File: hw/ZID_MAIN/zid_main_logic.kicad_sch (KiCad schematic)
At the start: 82 parts, among them J1 Conn_01x02_Pin_2.54mm, J2 Conn_02x05_2.54mm, J3 Conn_02x05_2.54mm, J4 Conn_02x05_PINHDR_2.54mm, J5 HDR 1x04 Socket, J6 Conn_02x03_Odd_Even, J7 Conn_01x03, M1 WS-RP2040-Zero, SW1 SW_Push, SW2 SW_DIP_x02, U1 74HCT161, U10 74FCT2245, U11 SST39SF010, U12 AS7C1024B-10J, U13 74FCT541C, U14 74AHCT244, U15 74FCT257T, U16 74HCT166, U17 74HCT166, U18 74LVC245, U19 74LVC125AS, U2 74FCT541C, U20 24LC32, U21 ATF1504AS-44T, U22 74AHCT1G125, U23 74LVC273, U25 74LVC3G04, U3 74FCT541C, U4 MIC2775, U5 OSC-20MHz, U6 Z80 C20MHz-PLCC, U7 ATF1508AS, U8 74FCT2245, U9 74FCT2245

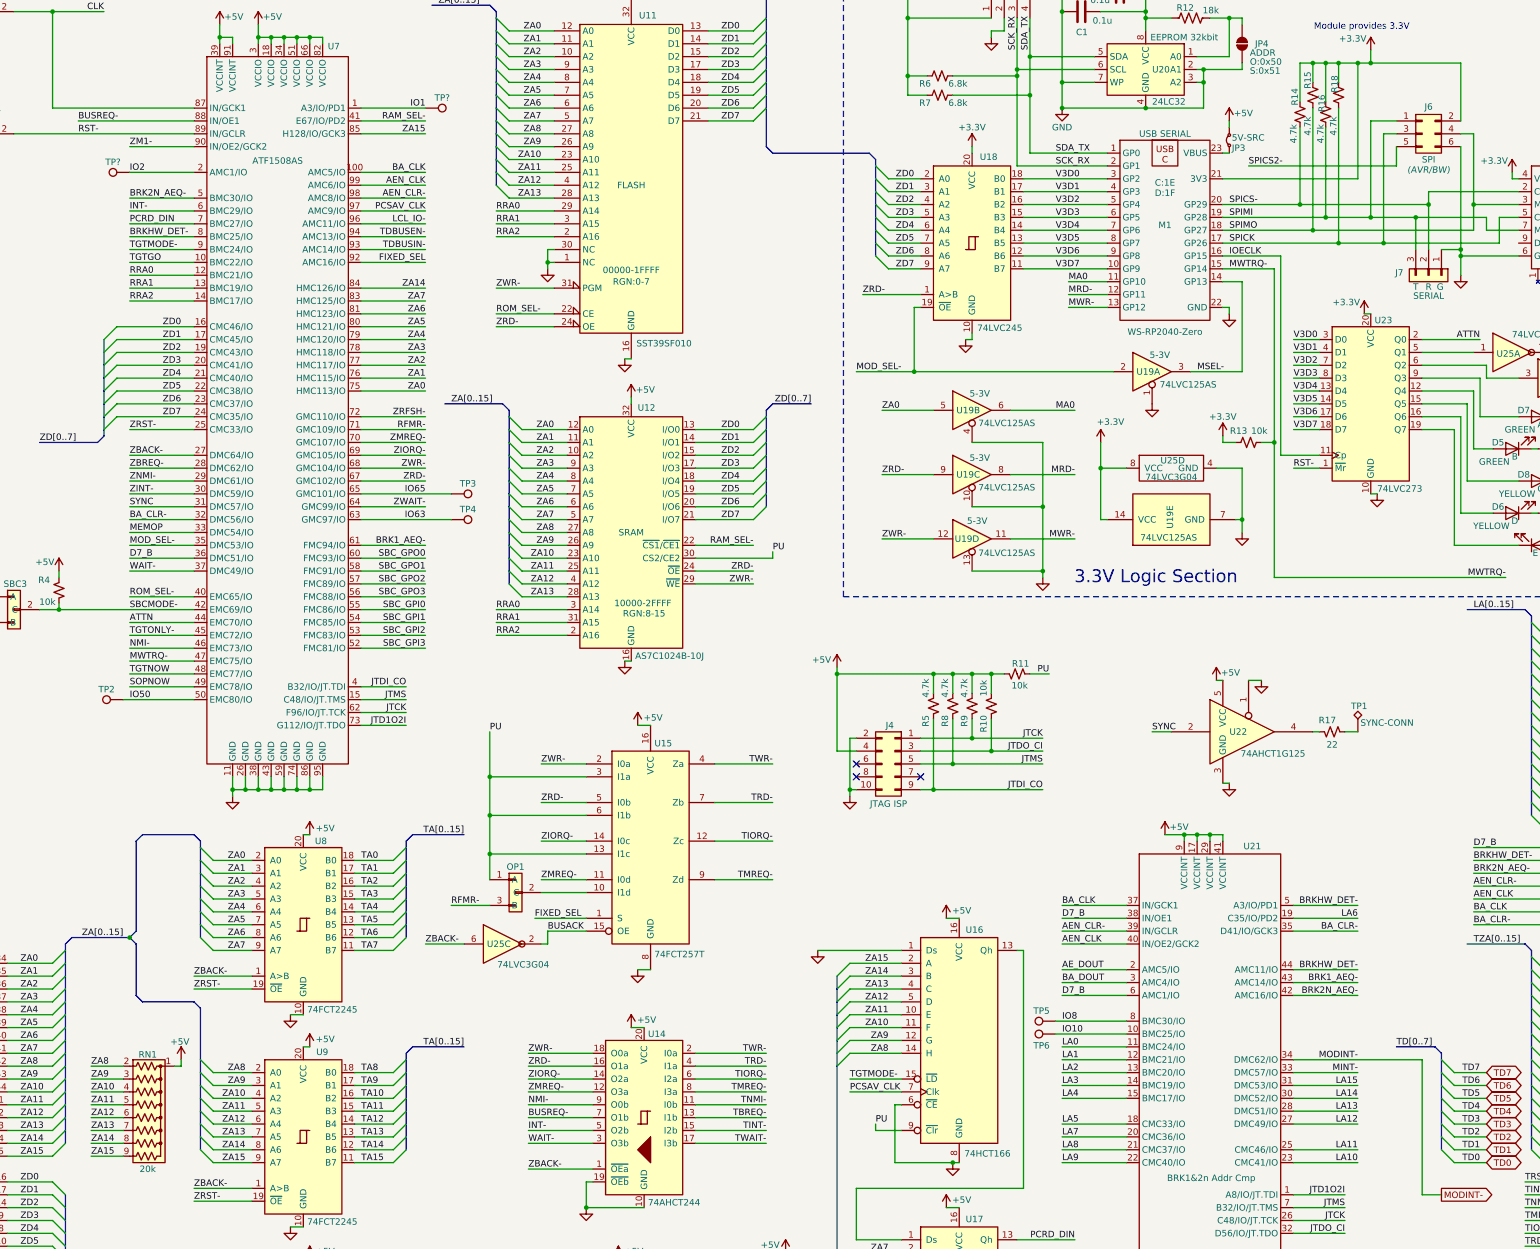
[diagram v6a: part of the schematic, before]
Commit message: Break exp conn 2x20
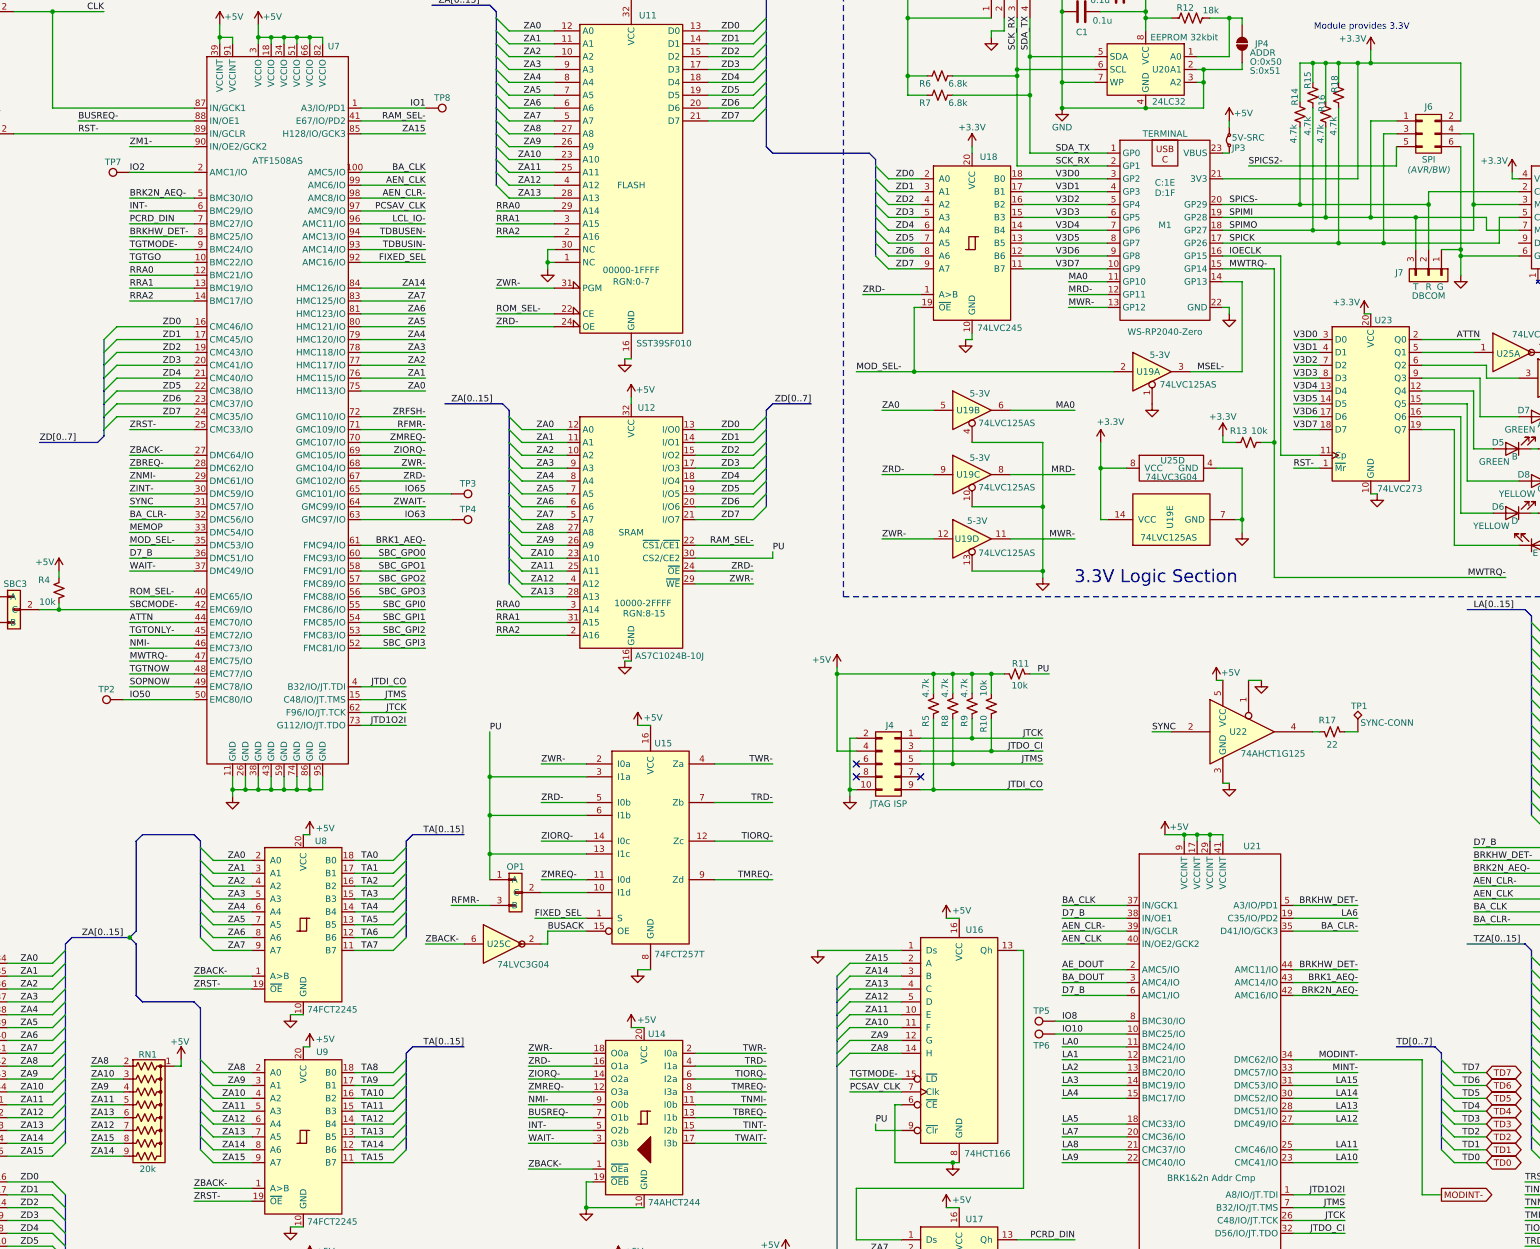
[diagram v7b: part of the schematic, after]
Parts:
- J7: Function SERIAL -> DBCOM
- M1: Function USB SERIAL -> TERMINAL
- OP1: Function (none) -> TGT-MREQ; OP-A (none) -> NOMR; OP-B (none) -> RFMR
- gave numbers to parts that had none: 2
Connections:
- net ZA10: now also RN1.3 (R2); no longer RN1.4 (R3)
- net ZA12: now also RN1.7 (R6); no longer RN1.6 (R5)
- net ZA13: now also RN1.6 (R5); no longer RN1.7 (R6)
- net ZA14: now also RN1.9 (R8); no longer RN1.8 (R7)
- net ZA15: now also RN1.8 (R7); no longer RN1.9 (R8)
- net ZA9: now also RN1.4 (R3); no longer RN1.3 (R2)
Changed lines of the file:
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@@
 		)
 	)
+	(label "ZA15"
+		(at 100.33 245.11 0)
+		(effects
+			(font
+				(size 1.27 1.27)
+			)
+			(justify left bottom)
+		)
+	)
 	(label "MWTRQ-"
 		(at 325.12 72.39 0)
@@
 		)
 	)
-	(label "ZA10"
-		(at 100.33 234.95 0)
-		(effects
-			(font
-				(size 1.27 1.27)
-			)
-			(justify left bottom)
-		)
-	)
 	(label "ZD1"
 		(at 86.36 255.27 0)
@@
 		)
 	)
-	(label "ZA9"
-		(at 100.33 232.41 0)
-		(effects
-			(font
-				(size 1.27 1.27)
-			)
-			(justify left bottom)
-		)
-	)
 	(label "ZA6"
 		(at 189.23 40.64 180)
@@
 		)
 	)
+	(label "ZA10"
+		(at 100.33 232.41 0)
+		(effects
+			(font
+				(size 1.27 1.27)
+			)
+			(justify left bottom)
+		)
+	)
 	(label "ZWAIT-"
 		(at 166.37 119.38 180)
@@
 		)
 	)
-	(label "ZA13"
-		(at 100.33 242.57 0)
-		(effects
-			(font
-				(size 1.27 1.27)
-			)
-			(justify left bottom)
-		)
-	)
 	(label "LA3"
 		(at 393.7 175.26 180)
@@
 		)
 	)
+	(label "ZA13"
+		(at 100.33 240.03 0)
+		(effects
+			(font
+				(size 1.27 1.27)
+			)
+			(justify left bottom)
+		)
+	)
 	(label "JTDO_CI"
 		(at 288.29 167.64 180)
@@
 		)
 	)
+	(label "ZA9"
+		(at 100.33 234.95 0)
+		(effects
+			(font
+				(size 1.27 1.27)
+			)
+			(justify left bottom)
+		)
+	)
 	(label "TIORQ-"
 		(at 383.54 262.89 0)
@@
 		)
 	)
+	(label "ZA12"
+		(at 100.33 242.57 0)
+		(effects
+			(font
+				(size 1.27 1.27)
+			)
+			(justify left bottom)
+		)
+	)
 	(label "TA5"
 		(at 393.7 236.22 180)
@@
 		)
 	)
-	(label "ZA14"
-		(at 100.33 245.11 0)
-		(effects
-			(font
-				(size 1.27 1.27)
-			)
-			(justify left bottom)
-		)
-	)
 	(label "ZA15"
 		(at 166.37 45.72 180)
@@
 		)
 	)
-	(label "ZA12"
-		(at 100.33 240.03 0)
-		(effects
-			(font
-				(size 1.27 1.27)
-			)
-			(justify left bottom)
-		)
-	)
 	(label "ZA15"
 		(at 257.81 209.55 180)
@@
 		)
 	)
-	(label "ZA15"
-		(at 100.33 247.65 0)
-		(effects
-			(font
-				(size 1.27 1.27)
-			)
-			(justify left bottom)
-		)
-	)
 	(label "TA1"
 		(at 393.7 246.38 180)
@@
 		)
 	)
+	(label "ZA14"
+		(at 100.33 247.65 0)
+		(effects
+			(font
+				(size 1.27 1.27)
+			)
+			(justify left bottom)
+		)
+	)
 	(label "RAM_SEL-"
 		(at 166.37 43.18 180)
@@
 			)
 		)
-		(property "Function" "SERIAL"
+		(property "Function" "DBCOM"
 			(at 364.49 77.724 90)
 			(effects
@@
 			)
 		)
+		(property "OP-A" "NOMR"
+			(at 184.15 190.5 0)
+			(effects
+				(font
+					(size 1.27 1.27)
+				)
+				(hide yes)
+			)
+		)
+		(property "OP-B" "RFMR"
+			(at 184.15 190.5 0)
+			(effects
+				(font
+					(size 1.27 1.27)
+				)
+				(hide yes)
+			)
+		)
+		(property "Function" "TGT-MREQ"
+			(at 184.15 190.5 0)
+			(effects
+				(font
+					(size 1.27 1.27)
+				)
+				(hide yes)
+			)
+		)
 		(pin "3"
 		)
@@
 		(on_board yes)
 		(dnp no)
-		(property "Reference" "TP?"
+		(property "Reference" "TP7"
 			(at 104.648 51.308 90)
 			(effects
@@
 			(project "ZID_MAIN"
 				(path "/2be47242-6db6-4d8d-b590-8c682dee013e/f092485f-e7d4-42be-add8-9bafec004ccb"
-					(reference "TP?")
+					(reference "TP7")
 					(unit 1)
 				)
@@
 			)
 		)
-		(property "Function" "USB SERIAL"
+		(property "Function" "TERMINAL"
 			(at 312.42 45.72 0)
 			(effects
@@
 		(on_board yes)
 		(dnp no)
-		(property "Reference" "TP?"
+		(property "Reference" "TP8"
 			(at 169.672 38.608 90)
 			(effects
@@
 			(project "ZID_MAIN"
 				(path "/2be47242-6db6-4d8d-b590-8c682dee013e/f092485f-e7d4-42be-add8-9bafec004ccb"
-					(reference "TP?")
+					(reference "TP8")
 					(unit 1)
 				)

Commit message: PCB comp place #1
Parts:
- removed JP2: Jumper_2_Small_Open, Connector_PinHeader_2.00mm:PinHeader_1x02_P2.00mm_Vertical, symbol Jumper:Jumper_2_Small_Open
- added JP2: Jumper_2_Small_Open_wsto-AES, Connector_PinHeader_2.00mm:PinHeader_1x03_P2.00mm_Vertical, symbol AES_Library:Jumper_2_Small_Open_wsto-AES
- J1: Function Ext-RST -> RST PB
- JP1: OP1-2 (none) -> OPEN; OP2-3 (none) -> EXPRST
- SW1: Function (none) -> RESET
- TP1: Function (none) -> SYNC
- TP2: Function CPLD Pin Available -> IO50
- TP3: Function CPLD Pin Available -> IO65
- TP4: Function CPLD Pin Available -> IO63
- TP5: Function CPLD Pin Available -> IO8
- TP6: Function CPLD Pin Available -> IO10
- TP7: Function CPLD Pin Available -> IO2
- TP8: Function CPLD Pin Available -> IO1
- U5: Freq (none) -> 20MHz(max)
- U7: Function (none) -> MAIN LOGIC
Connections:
- net TA0: now also U8.11 (B7); no longer U8.18 (B0)
- net TA1: now also U8.12 (B6); no longer U8.17 (B1)
- net TA10: now also U9.13 (B5); no longer U9.16 (B2)
- net TA11: now also U9.14 (B4); no longer U9.15 (B3)
- net TA12: now also U9.15 (B3); no longer U9.14 (B4)
- net TA13: now also U9.16 (B2); no longer U9.13 (B5)
- net TA14: now also U9.17 (B1); no longer U9.12 (B6)
- net TA15: now also U9.18 (B0); no longer U9.11 (B7)
- net TA2: now also U8.13 (B5); no longer U8.16 (B2)
- net TA3: now also U8.14 (B4); no longer U8.15 (B3)
- net TA4: now also U8.15 (B3); no longer U8.14 (B4)
- net TA5: now also U8.16 (B2); no longer U8.13 (B5)
- net TA6: now also U8.17 (B1); no longer U8.12 (B6)
- net TA7: now also U8.18 (B0); no longer U8.11 (B7)
- net TA8: now also U9.11 (B7); no longer U9.18 (B0)
- net TA9: now also U9.12 (B6); no longer U9.17 (B1)
- net TCLK: now also JP2.3 (C)
- net TRST-: now also JP1.3 (C); no longer JP1.1 (A)
- net ZA0: now also U8.9 (A7); no longer U8.2 (A0)
- net ZA1: now also U8.8 (A6); no longer U8.3 (A1)
- net ZA10: now also RN1.4 (R3), U9.7 (A5); no longer RN1.3 (R2), U9.4 (A2)
- net ZA11: now also U9.6 (A4); no longer U9.5 (A3)
- net ZA12: now also RN1.6 (R5), U9.5 (A3); no longer RN1.7 (R6), U9.6 (A4)
- net ZA13: now also RN1.7 (R6), U9.4 (A2); no longer RN1.6 (R5), U9.7 (A5)
- net ZA14: now also RN1.8 (R7), U9.3 (A1); no longer RN1.9 (R8), U9.8 (A6)
- net ZA15: now also RN1.9 (R8), U9.2 (A0); no longer RN1.8 (R7), U9.9 (A7)
- net ZA2: now also U8.7 (A5); no longer U8.4 (A2)
- net ZA3: now also U8.6 (A4); no longer U8.5 (A3)
- net ZA4: now also U8.5 (A3); no longer U8.6 (A4)
- net ZA5: now also U8.4 (A2); no longer U8.7 (A5)
- net ZA6: now also U8.3 (A1); no longer U8.8 (A6)
- net ZA7: now also U8.2 (A0); no longer U8.9 (A7)
- net ZA8: now also U9.9 (A7); no longer U9.2 (A0)
- net ZA9: now also RN1.3 (R2), U9.8 (A6); no longer RN1.4 (R3), U9.3 (A1)
- net _CLK: now also JP2.2 (B)
- no-connect marks 9 -> 10
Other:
- moved on the sheet: JP1
